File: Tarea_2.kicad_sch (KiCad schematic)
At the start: 3 parts, among them J1 54-00166, J2 PPTC241LFBN-RC, U2 TPS75318QPWPRQ1

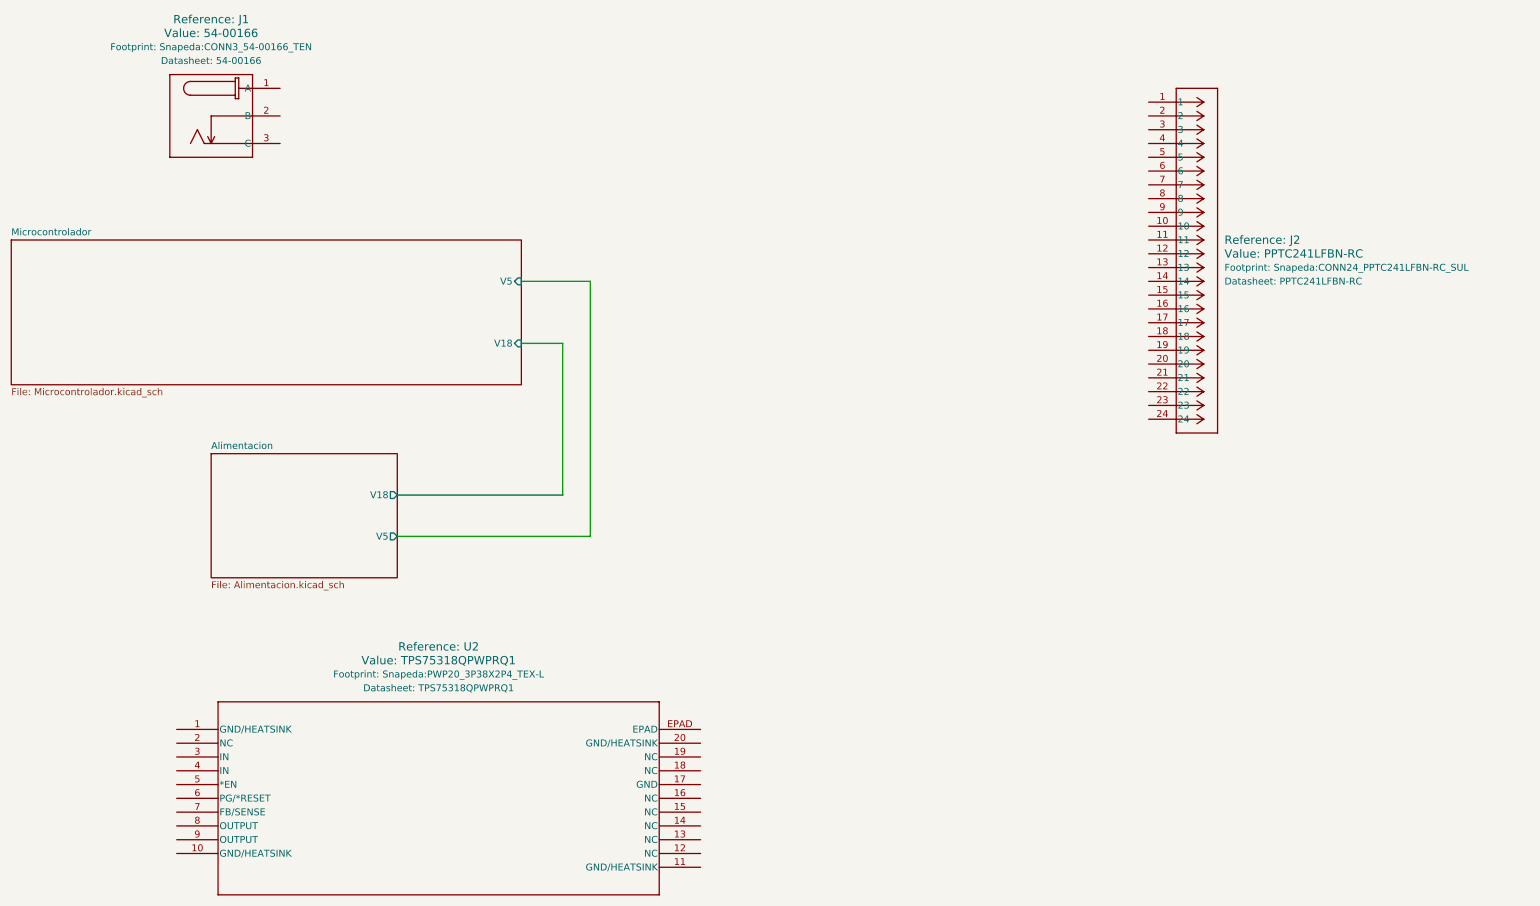
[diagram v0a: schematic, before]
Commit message: Branch Alimentacion 1.1 Modificaciones para que la alimentacion sea adecuada.
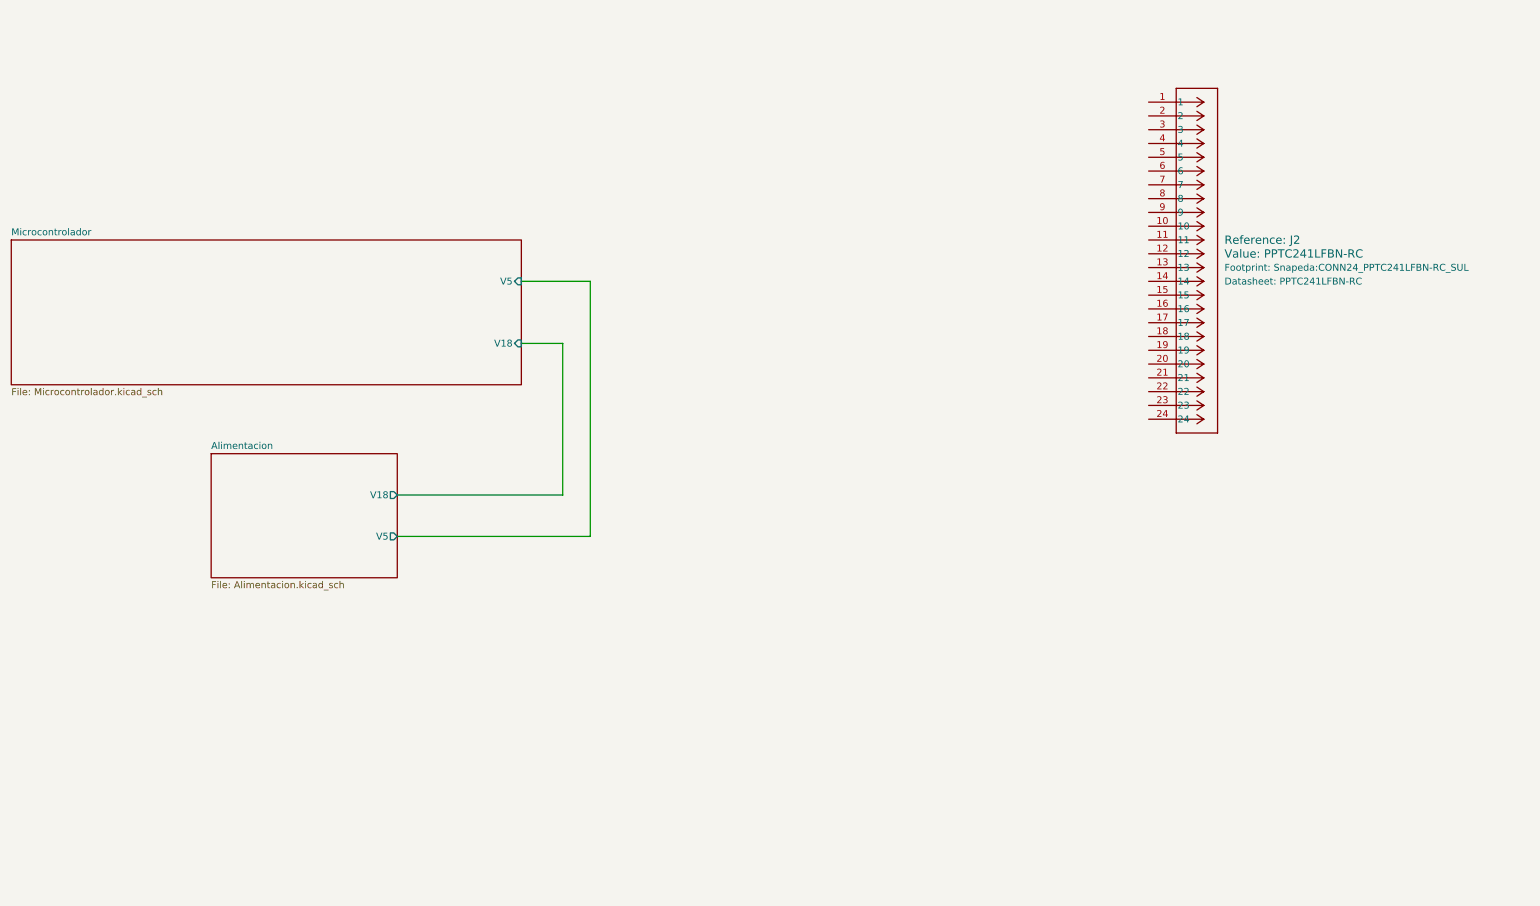
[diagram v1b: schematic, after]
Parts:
- removed J1: 54-00166, Snapeda:CONN3_54-00166_TEN, symbol Snapeda:54-00166
- removed U2: TPS75318QPWPRQ1, Snapeda:PWP20_3P38X2P4_TEX-L, symbol Snapeda:TPS75318QPWPRQ1
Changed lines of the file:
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@@
-		)
-	)
-	(symbol
-		(lib_id "Snapeda:TPS75318QPWPRQ1")
-		(at 71.12 163.83 0)
-		(unit 1)
-		(body_style 1)
-		(exclude_from_sim no)
-		(in_bom yes)
-		(on_board yes)
-		(in_pos_files yes)
-		(dnp no)
-		(fields_autoplaced yes)
-		(property "Reference" "U2"
-			(at 119.38 148.59 0)
-			(show_name yes)
-			(do_not_autoplace no)
-			(effects
-				(font
-					(size 1.524 1.524)
-				)
-			)
-		)
-		(property "Value" "TPS75318QPWPRQ1"
-			(at 119.38 151.13 0)
-			(show_name yes)
-			(do_not_autoplace no)
-			(effects
-				(font
-					(size 1.524 1.524)
-				)
-			)
-		)
-		(property "Footprint" "Snapeda:PWP20_3P38X2P4_TEX-L"
-			(at 119.38 153.67 0)
-			(show_name yes)
-			(do_not_autoplace no)
-			(effects
-				(font
-					(size 1.27 1.27)
-				)
-			)
-		)
-		(property "Datasheet" "TPS75318QPWPRQ1"
-			(at 119.38 156.21 0)
-			(show_name yes)
-			(do_not_autoplace no)
-			(effects
-				(font
-					(size 1.27 1.27)
-				)
-			)
-		)
-		(property "Description" ""
-			(at 71.12 163.83 0)
-			(show_name yes)
-			(do_not_autoplace no)
-			(effects
-				(font
-					(size 1.27 1.27)
-				)
-			)
-		)
-		(pin "1"
-		)
-		(pin "9"
-		)
-		(pin "13"
-		)
-		(pin "12"
-		)
-		(pin "10"
-		)
-		(pin "11"
-		)
-		(pin "2"
-		)
-		(pin "19"
-		)
-		(pin "EPAD"
-		)
-		(pin "18"
-		)
-		(pin "6"
-		)
-		(pin "20"
-		)
-		(pin "16"
-		)
-		(pin "14"
-		)
-		(pin "8"
-		)
-		(pin "15"
-		)
-		(pin "7"
-		)
-		(pin "4"
-		)
-		(pin "17"
-		)
-		(pin "5"
-		)
-		(pin "3"
-		)
-		(instances
-			(project "Tarea_2"
-				(path "/9f5ae3b6-454f-40a7-b9eb-0aa1aaaab031"
-					(reference "U2")
-					(unit 1)
-				)
-			)
-		)
-	)
-	(symbol
-		(lib_id "Snapeda:54-00166")
-		(at 90.17 45.72 0)
-		(unit 1)
-		(body_style 1)
-		(exclude_from_sim no)
-		(in_bom yes)
-		(on_board yes)
-		(in_pos_files yes)
-		(dnp no)
-		(fields_autoplaced yes)
-		(property "Reference" "J1"
-			(at 77.47 33.02 0)
-			(show_name yes)
-			(do_not_autoplace no)
-			(effects
-				(font
-					(size 1.524 1.524)
-				)
-			)
-		)
-		(property "Value" "54-00166"
-			(at 77.47 35.56 0)
-			(show_name yes)
-			(do_not_autoplace no)
-			(effects
-				(font
-					(size 1.524 1.524)
-				)
-			)
-		)
-		(property "Footprint" "Snapeda:CONN3_54-00166_TEN"
-			(at 77.47 38.1 0)
-			(show_name yes)
-			(do_not_autoplace no)
-			(effects
-				(font
-					(size 1.27 1.27)
-				)
-			)
-		)
-		(property "Datasheet" "54-00166"
-			(at 77.47 40.64 0)
-			(show_name yes)
-			(do_not_autoplace no)
-			(effects
-				(font
-					(size 1.27 1.27)
-				)
-			)
-		)
-		(property "Description" ""
-			(at 90.17 45.72 0)
-			(show_name yes)
-			(do_not_autoplace no)
-			(effects
-				(font
-					(size 1.27 1.27)
-				)
-			)
-		)
-		(pin "2"
-		)
-		(pin "1"
-		)
-		(pin "3"
-		)
-		(instances
-			(project "Tarea_2"
-				(path "/9f5ae3b6-454f-40a7-b9eb-0aa1aaaab031"
-					(reference "J1")
-					(unit 1)
-				)
-			)
 		)
 	)

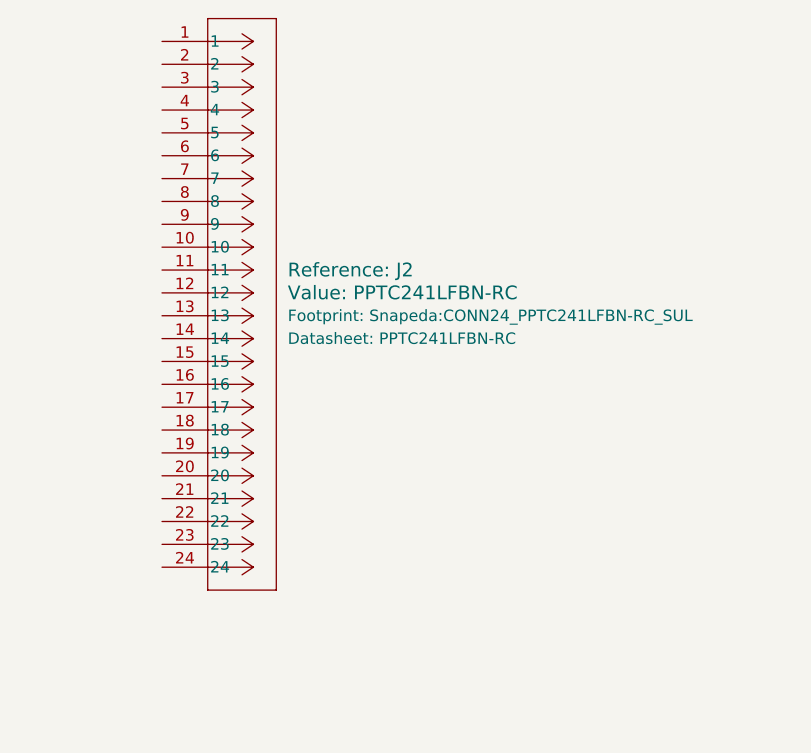
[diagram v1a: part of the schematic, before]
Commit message: branch microcontrolador 1.1
Modificaciones iniciales de la subhoja del micro
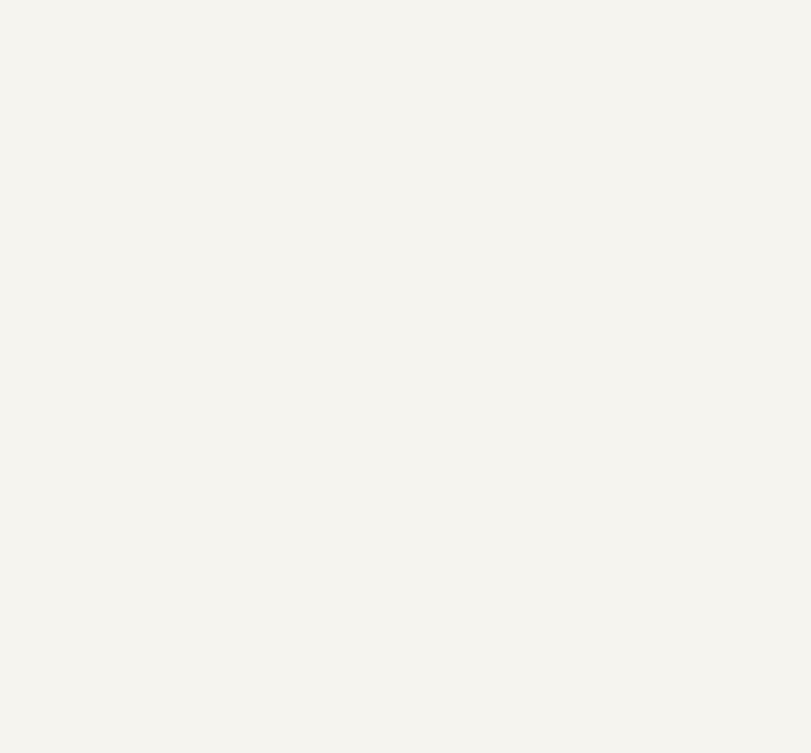
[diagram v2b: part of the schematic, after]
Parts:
- removed J2: PPTC241LFBN-RC, Snapeda:CONN24_PPTC241LFBN-RC_SUL, symbol Snapeda:PPTC241LFBN-RC
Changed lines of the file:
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@@
-		)
-	)
-	(symbol
-		(lib_id "Snapeda:PPTC241LFBN-RC")
-		(at 250.19 48.26 0)
-		(unit 1)
-		(body_style 1)
-		(exclude_from_sim no)
-		(in_bom yes)
-		(on_board yes)
-		(in_pos_files yes)
-		(dnp no)
-		(fields_autoplaced yes)
-		(property "Reference" "J2"
-			(at 264.16 73.6599 0)
-			(show_name yes)
-			(do_not_autoplace no)
-			(effects
-				(font
-					(size 1.524 1.524)
-				)
-				(justify left)
-			)
-		)
-		(property "Value" "PPTC241LFBN-RC"
-			(at 264.16 76.1999 0)
-			(show_name yes)
-			(do_not_autoplace no)
-			(effects
-				(font
-					(size 1.524 1.524)
-				)
-				(justify left)
-			)
-		)
-		(property "Footprint" "Snapeda:CONN24_PPTC241LFBN-RC_SUL"
-			(at 264.16 78.7399 0)
-			(show_name yes)
-			(do_not_autoplace no)
-			(effects
-				(font
-					(size 1.27 1.27)
-				)
-				(justify left)
-			)
-		)
-		(property "Datasheet" "PPTC241LFBN-RC"
-			(at 264.16 81.2799 0)
-			(show_name yes)
-			(do_not_autoplace no)
-			(effects
-				(font
-					(size 1.27 1.27)
-				)
-				(justify left)
-			)
-		)
-		(property "Description" ""
-			(at 250.19 48.26 0)
-			(show_name yes)
-			(do_not_autoplace no)
-			(effects
-				(font
-					(size 1.27 1.27)
-				)
-			)
-		)
-		(pin "6"
-		)
-		(pin "4"
-		)
-		(pin "19"
-		)
-		(pin "18"
-		)
-		(pin "8"
-		)
-		(pin "24"
-		)
-		(pin "17"
-		)
-		(pin "21"
-		)
-		(pin "20"
-		)
-		(pin "5"
-		)
-		(pin "1"
-		)
-		(pin "2"
-		)
-		(pin "11"
-		)
-		(pin "15"
-		)
-		(pin "12"
-		)
-		(pin "13"
-		)
-		(pin "9"
-		)
-		(pin "22"
-		)
-		(pin "16"
-		)
-		(pin "23"
-		)
-		(pin "3"
-		)
-		(pin "7"
-		)
-		(pin "10"
-		)
-		(pin "14"
-		)
-		(instances
-			(project "Tarea_2"
-				(path "/9f5ae3b6-454f-40a7-b9eb-0aa1aaaab031"
-					(reference "J2")
-					(unit 1)
-				)
-			)
 		)
 	)
